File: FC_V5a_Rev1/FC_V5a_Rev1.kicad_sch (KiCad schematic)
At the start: 74 parts, among them IC2 AZ1117CH-3.3TRG1, IC3 RV-3028-C7_32.768kHz_1ppm_TA_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, J12 USB_C_Receptacle_USB2.0_16P, J16 DEBUG, J22 SWD Port, J3 Life Makes Lemonade, J4 Molex 503398-1892, J5 BM04B-SRSS-TB(LF)(SN), J6 Conn_Coaxial, J9 BM04B-SRSS-TB(LF)(SN), SW1 KMR2, SW2 KMR2, SW3 SW_Push_SPDT, U12 TCA9548ARGERQ1, U16 MCP9808T-E/MS, U30 E28-2G4M27S, U4 RFM98PW, U5 RFM9xBreakout, U7 LSM6DSOTR, U8 LSM303AGRTR

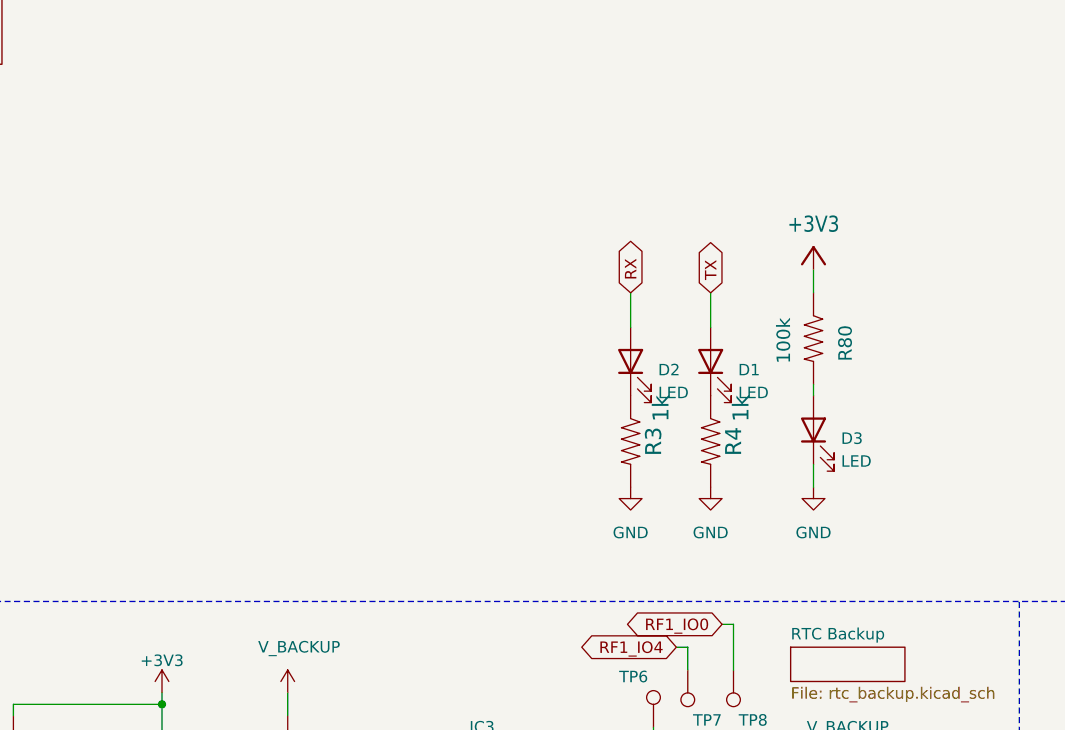
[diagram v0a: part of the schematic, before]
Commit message: Added CHRG and READONLY Sensing to GPIO Expander
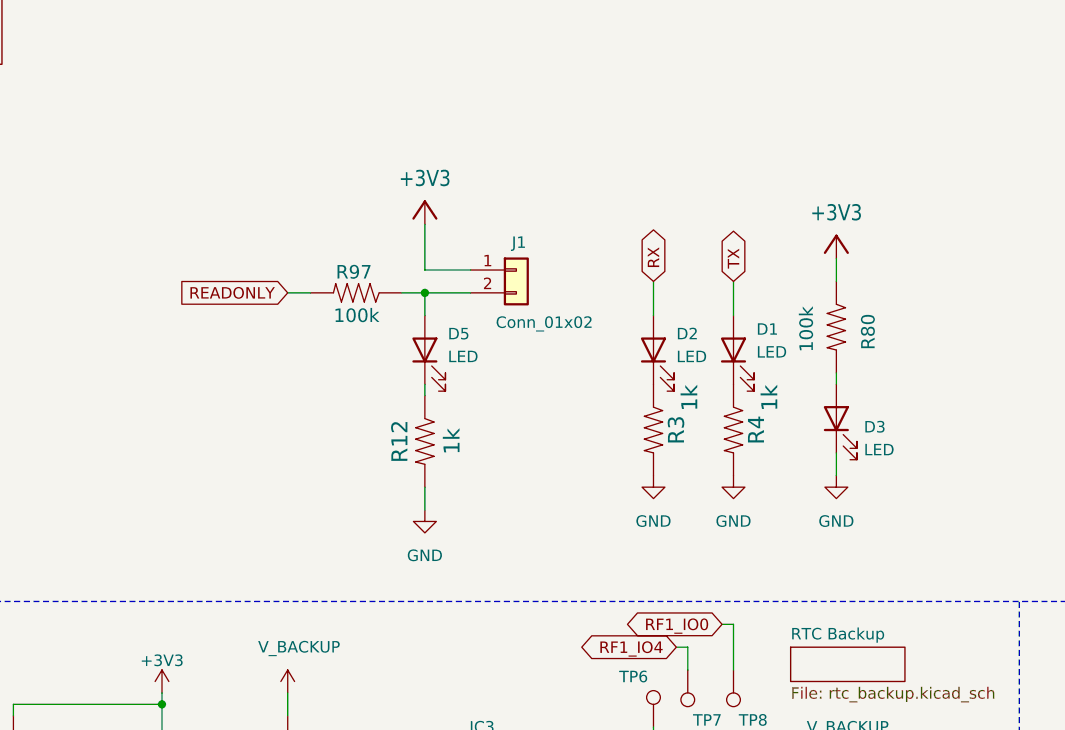
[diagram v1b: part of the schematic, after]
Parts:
- added D5: LED, LED_SMD:LED_0603_1608Metric, symbol Device:LED
- added J1: Conn_01x02, Connector_PinHeader_2.54mm:PinHeader_1x02_P2.54mm_Vertical, symbol Connector_Generic:Conn_01x02
- added R12: 1k, Resistor_SMD:R_0603_1608Metric, symbol mainboard:RESISTOR0603
- added R97: 100k, Resistor_SMD:R_0603_1608Metric, symbol mainboard:R-US_R0603
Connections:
- net +3V3: now also J1.1 (Pin_1)
- net GND: now also R12.2
- new net: D5.2 (A), J1.2 (Pin_2), R97.1
- new net: D5.1 (K), R12.1
- new net READONLY: R97.2
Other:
- moved on the sheet: D1, D2, D3, R3, R4, R80
